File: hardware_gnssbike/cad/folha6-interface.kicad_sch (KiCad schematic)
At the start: 22 parts, among them Q601 DMG1012T-7, Q602 DMG1012T-7, Q603 DMG1012T-7, SW601 XunPu TS-1088R-02026, SW602 XunPu TS-1088R-02026, SW603 XunPu TS-1088R-02026

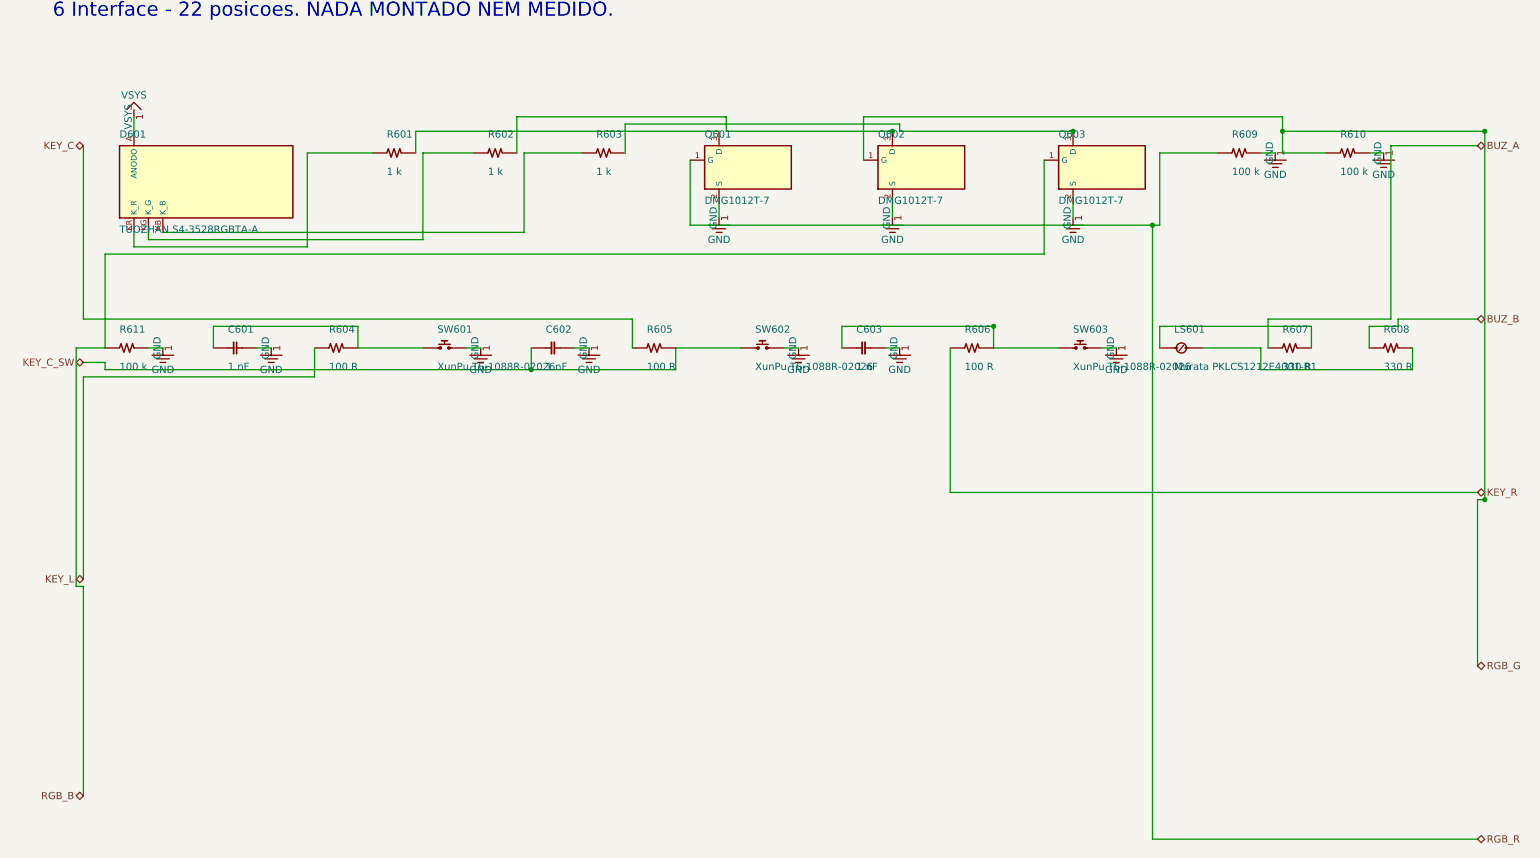
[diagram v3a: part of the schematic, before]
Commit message: feat(hardware): real symbols and real 3D models, from KiCad's own libraries
Two of the owner's asks in one commit, because they turned out to be the
same idea: stop drawing what already exists, reviewed, in the library.

THE SCHEMATIC. 36 of the parts were rectangles with pins around them - the
ICs, the connectors and the display - and a rectangle says nothing. Anyone
reading a schematic recognises a coaxial connector by the circle with the
dot, a switch by the contact that opens, a MOSFET by the channel and the
arrow.

ksym.py reads a symbol out of KiCad's own library - 21.110 of them, every
one reviewed against the KLC - and embeds it in our schematic with our
properties. simbolos.py says which part uses which. Eleven are in, and
ksym.checar() verifies every one pin number by pin number, because a
pretty symbol with the wire on the wrong pin is worse than a correct
rectangle. RF_GPS:MAX-M10S is literally our receiver: 18 pins, 18 names,
the same LCC-18.

Three symbols verify clean and still break the drawing, and they are
parked with the reason MEASURED rather than "did not work": the ADP5091
puts MPPT on the bottom edge beside its three ground pins and the ground
power symbol lands on the MPPT wire; the USB-C stacks four contacts per
point with 5,08 mm stubs and VBUS meets CC1; the ten pins of the display
FPC are all on one edge and two wires cannot reach. Each needs work
somewhere else - the power symbol placer, the placement - not a different
symbol.

Three bugs were found and fixed on the way, all in the router, all of the
same family: it assumed things about symbols that are only true of the
ones this project draws.

  - Symbols from KiCad are NOT centred on their origin. A
    Conn_01x10_Socket has its drawing at x -1,27 to 0 and all ten pins at
    x = -5,08. Treated as centred, pins fall inside the obstacle, the
    router cannot reach them from outside and goes over them instead -
    and two nets that touch are one net, with nothing in the drawing
    sa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
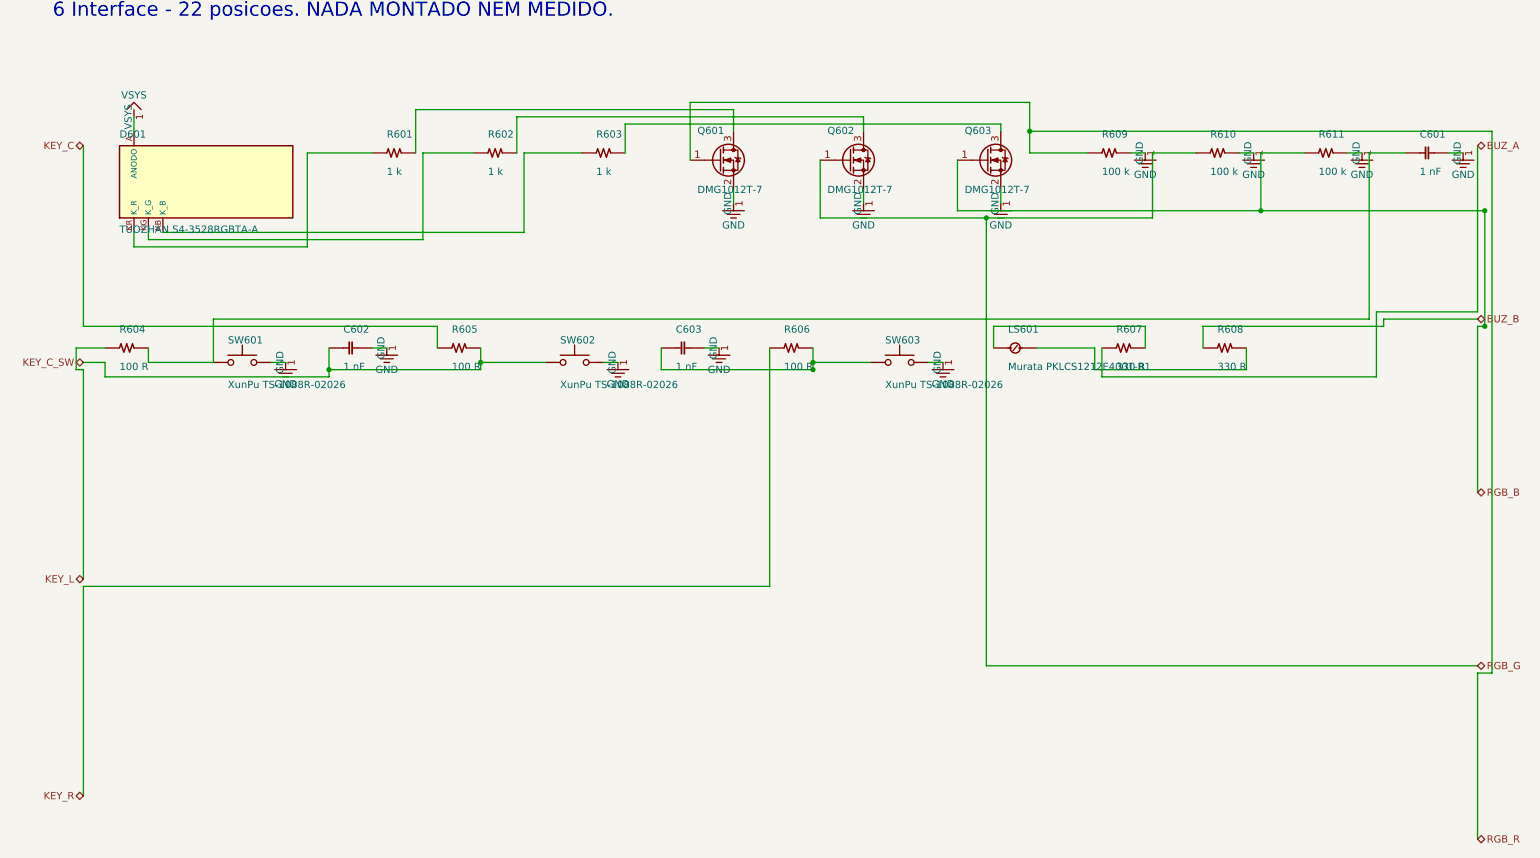
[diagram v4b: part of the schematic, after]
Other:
- moved on the sheet: C601, C602, C603, LS601, R604, R605, R606, R607, R608, R609, R610, R611

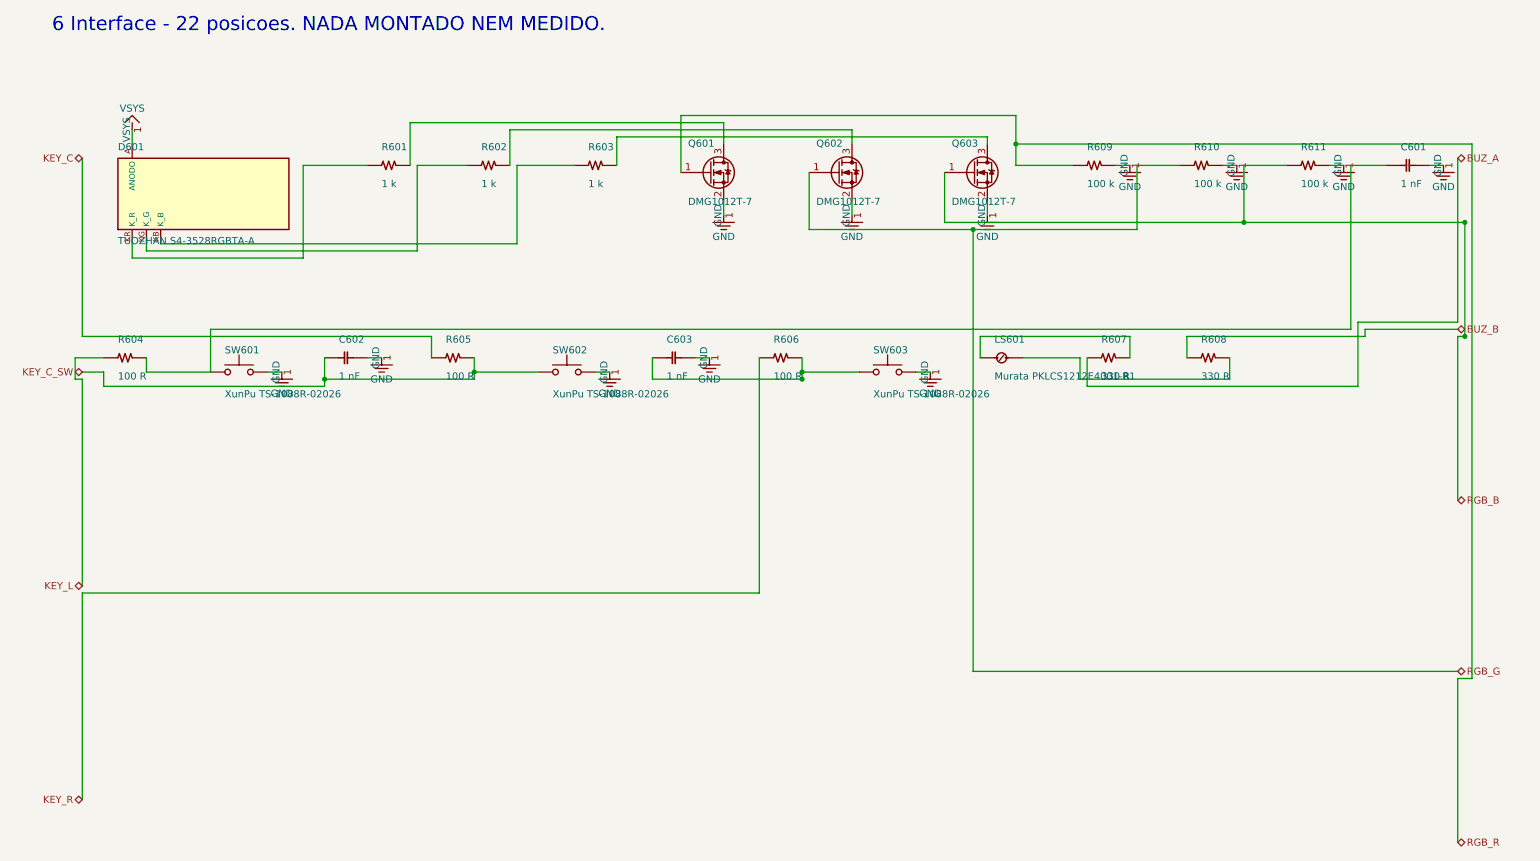
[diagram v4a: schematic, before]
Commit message: fix(hardware): the debug connector had RESET on the wrong contact
This one would have cost a board. The Tag-Connect TC2030 footprint had
pin 3 as no-connect and RESET on pin 6. The manufacturer's own data
sheet, TC2030-CTX_1.pdf, table "Connections", says the opposite: on the
six-pin footprint it is 3 = nRESET and 6 = SWO/TDO.

Where the mistake came from is worth writing down, because it is easy to
make twice: 1 VCC, 2 SWDIO, 3 GND, 4 SWCLK, 5 GND, 6 SWO is the
numbering of the ten-way Cortex header on the PROBE side, not of the
six-pin footprint on the board. Mixing the two gives exactly what was
written here.

What it would have done: the probe's nRESET is an open drain output, so
it would have driven nothing, and the MCU's reset would have hung off
the probe's SWO INPUT. Nothing burns - SWO runs target to probe, there
is no short - but the debugger can never reset the target: no connect
under reset, no pin reset. On an nRF54LM20A that reboots from task_wdt
or reconfigures its SWD pins, that removes the standard way out and
leaves only a full CTRL-AP erase.

The documentation carried a worse version still. 06 had GND on contact 3,
which fabricated would tie the probe's open-drain nRESET to copper
ground and hold the target in reset forever.

The project's own notes had predicted this exact variant - 06 carried a
CAUTION saying so and README an open checklist item. It was that one, and
it was caught before layout. Both are now closed, and the connector's
pin 6 is recorded as SWO with what is still unknown about it: which pad
of the ME54BS13 exposes SWO, which would give printf over ITM during
bring-up.

Fixed in parts.py, nets.py, 03-netlist.md, 06-conectores-e-pontos-de-teste.md,
07-sequencias-e-protecao.md and README.md.

Verified: check_sch and check_pcb pass, 78 of 78 diagrams render, 1529
links and none broken.
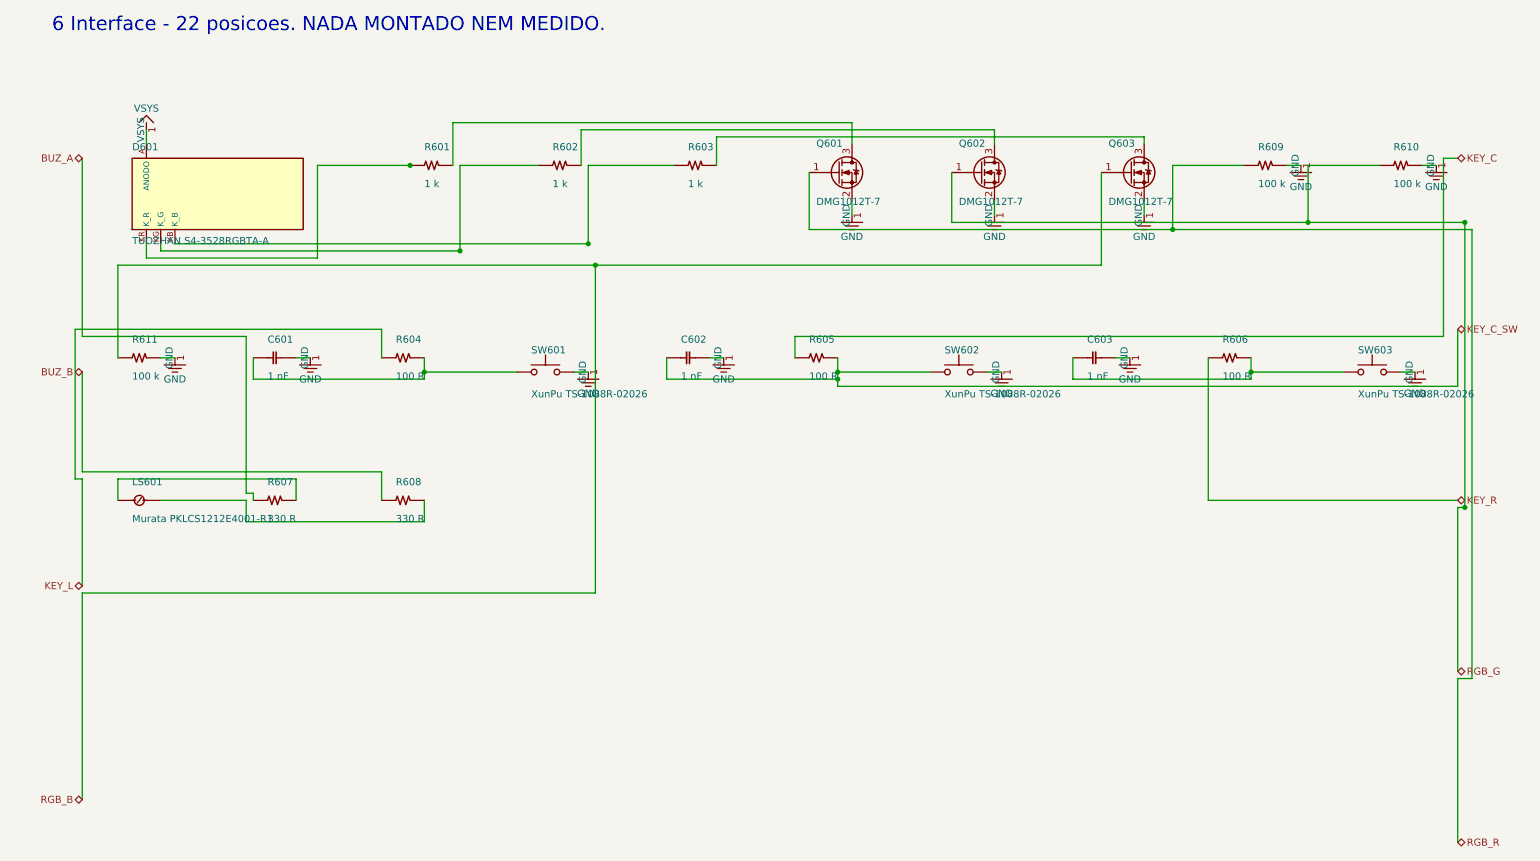
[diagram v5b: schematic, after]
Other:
- moved on the sheet: C601, C602, C603, D601, LS601, Q601, Q602, Q603, R601, R602, R603, R604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

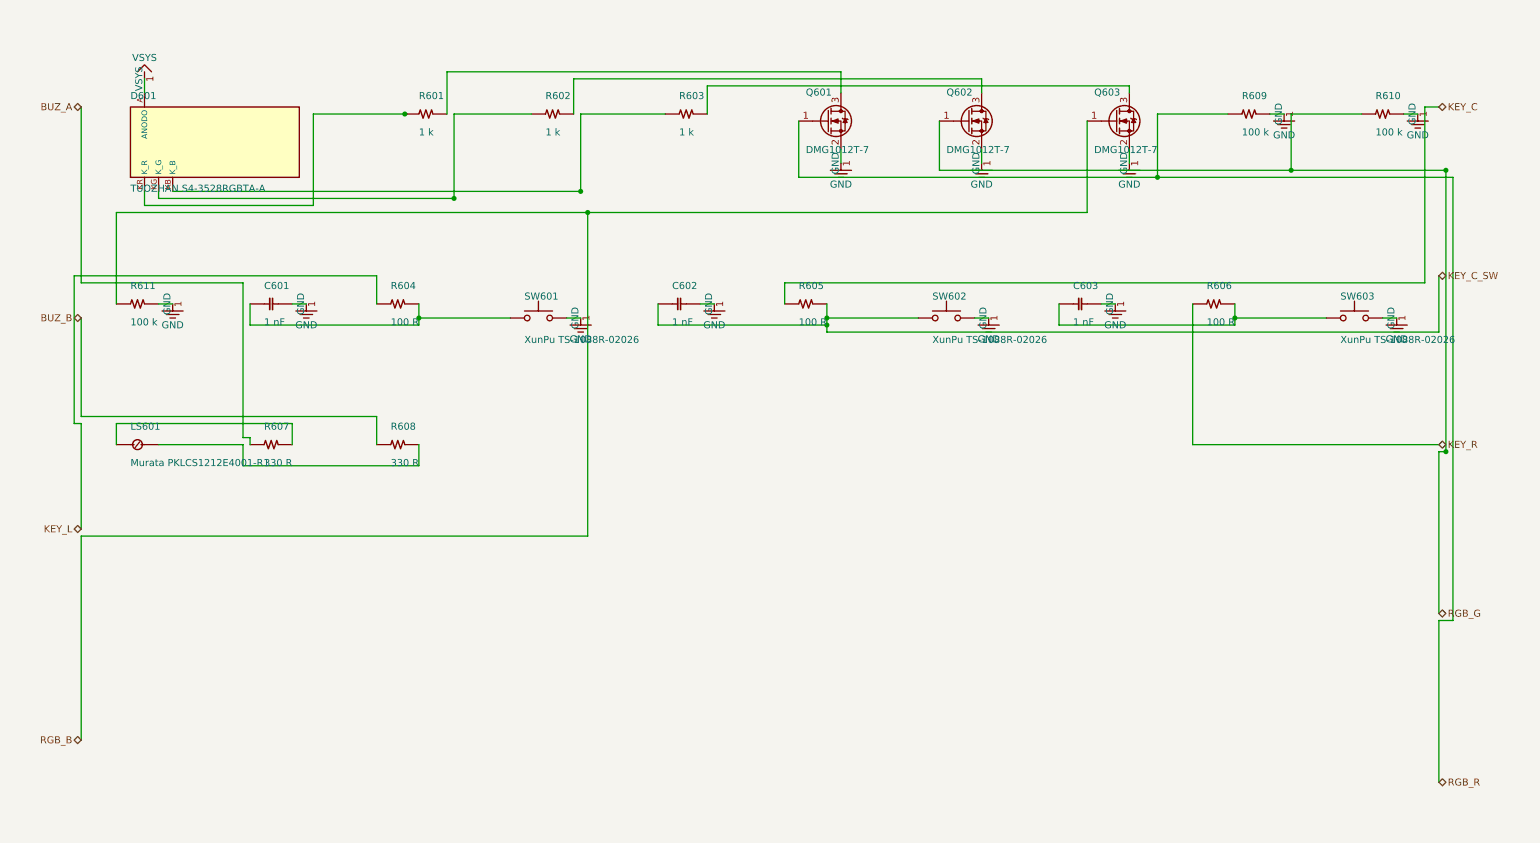
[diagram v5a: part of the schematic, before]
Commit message: feat(hardware): GNSS receiver on the 3V0 rail, and the electrical items closed with the owner
The receiver ran at 1.8 V from BUCK1 through a TXU0204 level shifter, and
table 35 of the MAX-F10S integration manual asks +-2 % of a 1.8 V supply
where the nPM1300 buck gives +-5 %. A +-1 % LDO from 3V0 fixed the
tolerance and cost 35 mW at the battery (the receiver paid at 3.0 V with
1.2 V burnt in the LDO); option 1 of the same table - VCC and V_IO tied at
3.0 V, VIO_SEL open - costs 11 mW and removes the shifter. The owner chose
option 1. The receiver now sits on 3V0 through JP103 and the ferrite, the
four digital lines go pin to pin, the shifter and the LDO leave with four
capacitors, and BUCK1 stays fitted and unloaded as in configuration 1 of
the nPM1300 datasheet (the datasheet only shows an unused BUCK2, and what
it does not show is not copied). The devicetree follows: vcc-supply on
BUCK2, BUCK1 regulator-boot-off. The receiver no longer has a rail that
switches off; that consequence is recorded in docs/10.

Closed the same day, each a decision of the owner or a datasheet fact:

  - the ADP5091 TERM and SETSD dividers hung from BAT with REF open;
    figure 42 of the datasheet hangs all four external dividers from REF,
    which the chip switches to BAT with the hysteresis resistor in series.
    Equation 6 did not hold as drawn. Net ADP_REF, same values.
  - the solar charge thermal cut-off: the ADP5091 has no temperature
    input and the NTC divider was on the board with nobody reading it. A
    TLV7031 fed from the panel compares RT101/R106 with half of SRC and
    pulls DIS_SW high through a BAT54WS, in diode-OR with the USB divider.
    Hot side only; charging below 0 C stays open, and says so.
  - the centre key reaches P1.27 through a Schottky (D107): the SHPHLD
    node rises to 5.5 V with the cable.
  - J102 copper matched to the pinout 06 sends to the pack maker: the
    copper had VBAT+ on 1, NTC on 4, GND on 6 and 2, 3 and 5 open.
  - FB301 with 150 mO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
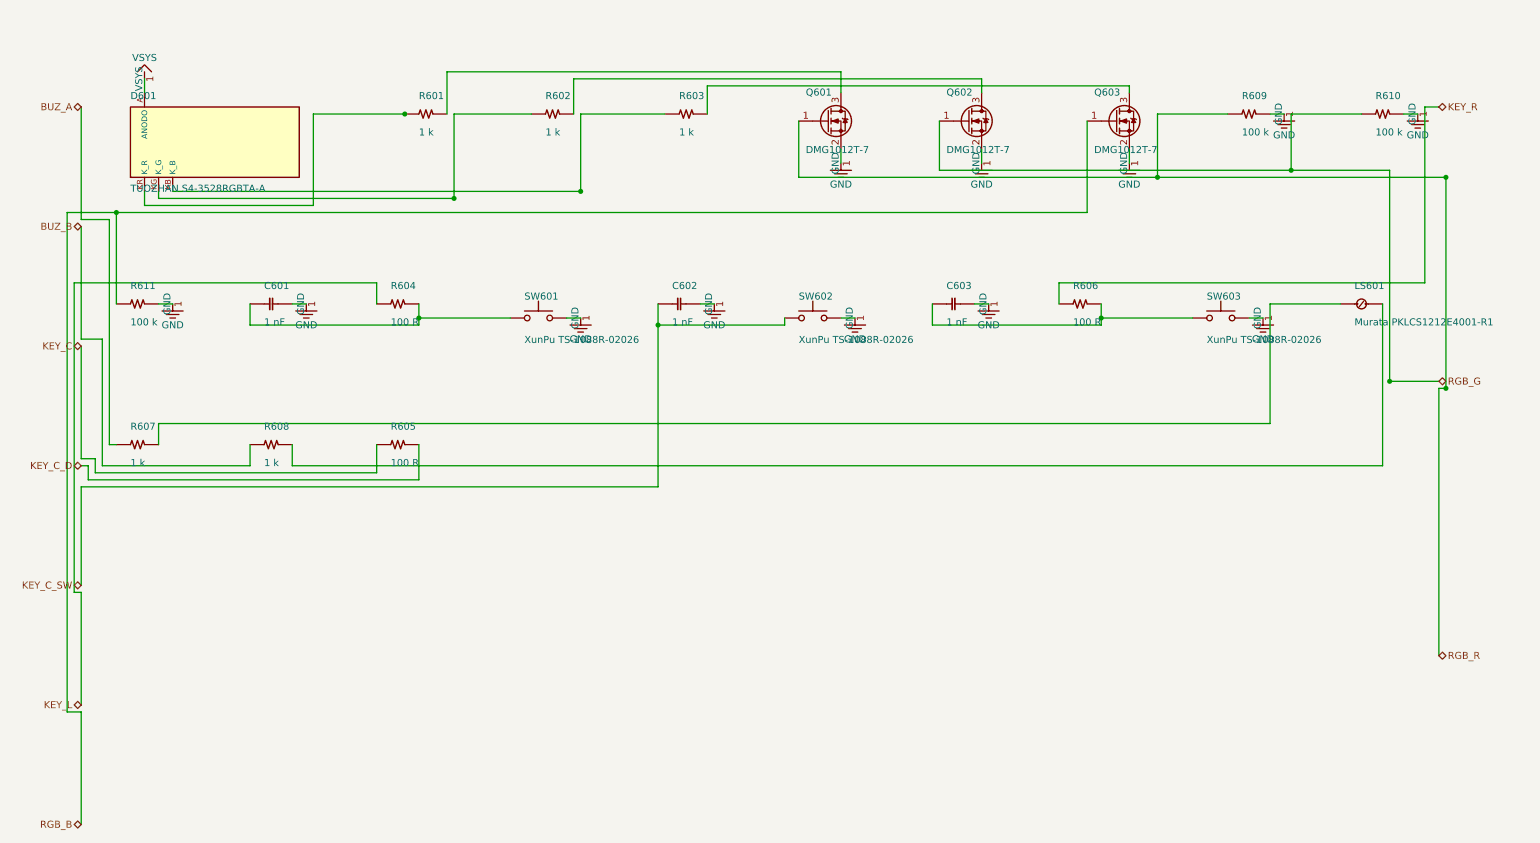
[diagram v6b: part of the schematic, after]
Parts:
- R607, R608: value 330 R -> 1 k
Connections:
- net KEY_C_SW: no longer R605.2
- new net KEY_C_D: R605.2
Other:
- moved on the sheet: C603, LS601, R605, R606, R607, R608, SW602, SW603
